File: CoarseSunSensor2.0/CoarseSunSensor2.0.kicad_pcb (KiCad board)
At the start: 2 copper layers, 45.4 x 14.2 mm, 23 parts, among them IC1 ADS1115IDGSR, J1 53261-0571

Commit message: Board repositioning
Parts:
- moved C1 36.7 mm to (137.8, 97.2)
- moved C2 36.7 mm to (143.6, 101.2)
- moved C4 36.7 mm to (132.2, 101.2)
- moved C6 36.7 mm to (154.5, 98.7)
- moved J1 36.7 mm to (161.3, 100.2)
- moved R4 36.7 mm to (132.2, 99.5)
- moved R6 36.7 mm to (162.8, 98.7)
- moved R8 36.7 mm to (162.8, 100.2)
- moved C5 36.7 mm to (154.5, 97.0)
- moved H1 36.7 mm to (124.0, 100.5)
- moved R1 36.7 mm to (137.8, 95.5)
- moved R5 36.7 mm to (151.2, 97.0)
- moved C3 36.7 mm to (136.9, 103.7)
- moved H2 36.7 mm to (154.6, 103.8)
- moved U1 36.7 mm to (137.6, 100.5)
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
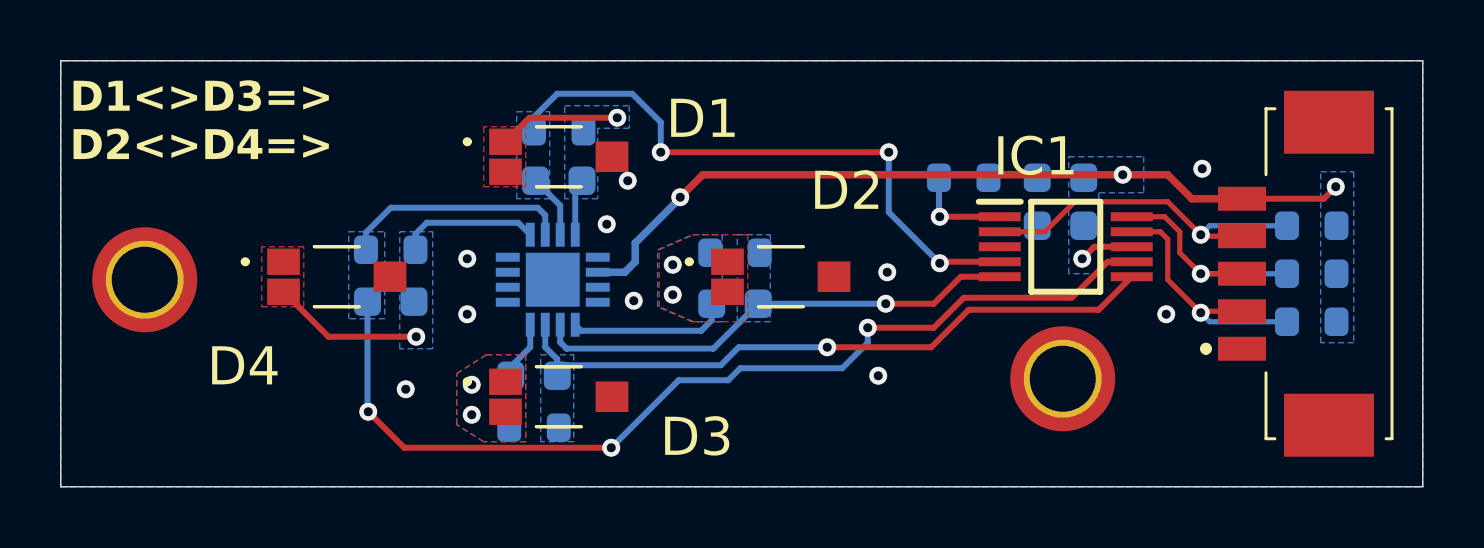
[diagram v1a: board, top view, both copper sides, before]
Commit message: Minor schematic changes
Calculei o valor dos capacitores e resistores
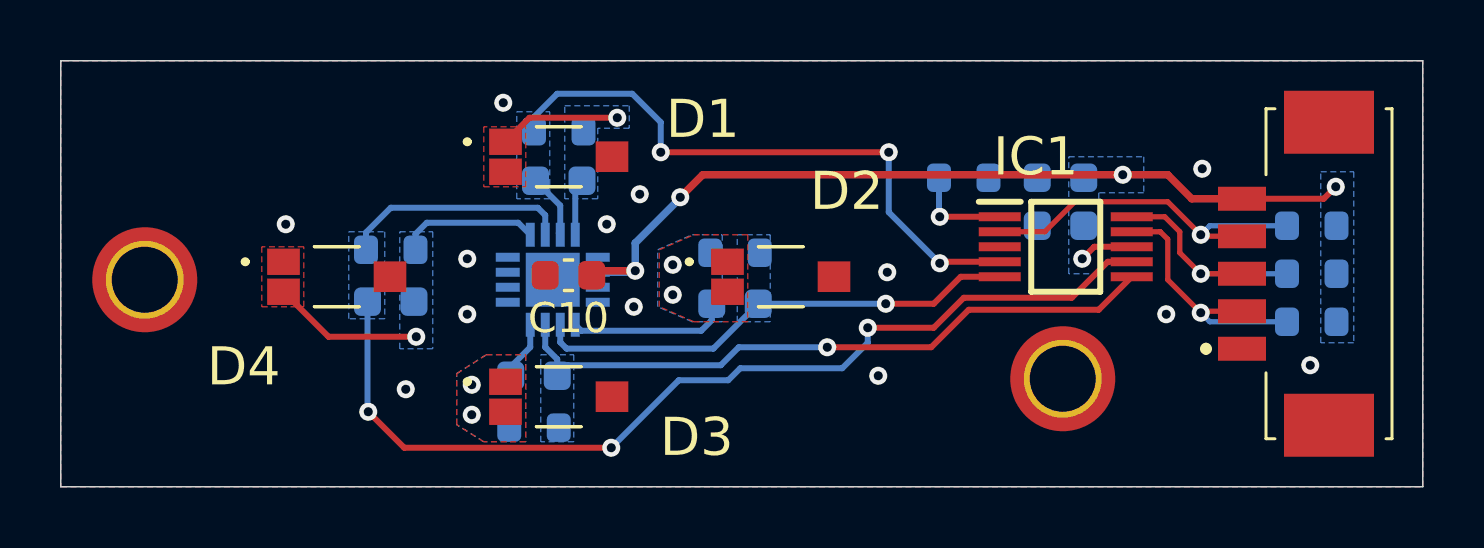
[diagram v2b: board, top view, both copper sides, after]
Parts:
- added C10: 10n, Capacitor_SMD:C_0603_1608Metric, F.Cu at (138.1, 100.3)
- C1, C2, C3, C4: value C -> 150p
- R1, R2, R3, R4: value R -> 95k
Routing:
- net +3V3: track 28.6 -> 30.3 mm, vias 4 -> 5
- net GND: vias 10 -> 13
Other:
- board text removed: "D1<>D3=> D2<>D4=>"
